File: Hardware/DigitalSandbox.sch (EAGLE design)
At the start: 82 parts, among them Q1 MOSFET-N, Q2 MOSFET-P, Q3 MOSFET-N, Q4 MOSFET-N, Q5 MOSFET-N, U1 MCP73831, U2 ATMEGA328, U3 C2031N-1A2-B10K-GP, U4 MCP9700, U5 FT232RLSSOP, U6 TEMT6000, U7 V_REG_LDOSMD, U8 LMV358, U9 MIC9.7MM, X1 USB-SMD-NS, Y1 8MHz

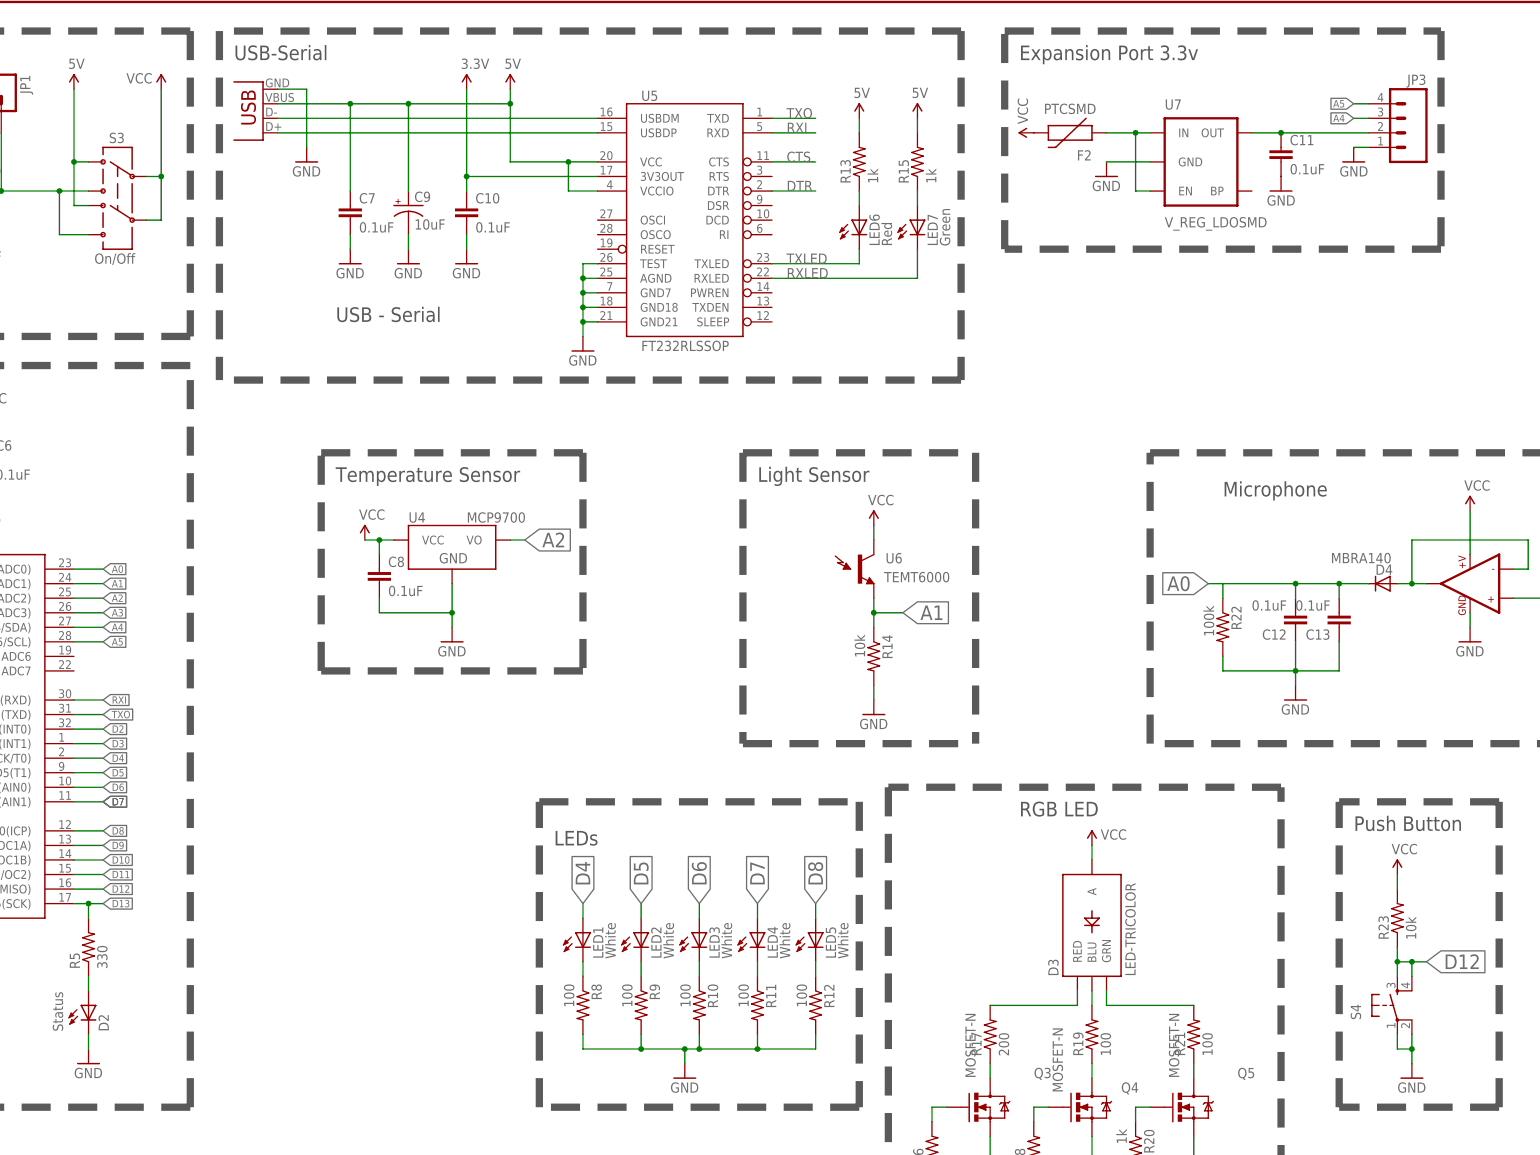
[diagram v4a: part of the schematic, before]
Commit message: Changes Made: 1. Swap Tx-Rx 3. correct stop mask on 2 exposed vias 6. flip default logic for push button (Currently normally high) 9. Change i2c header to meet new standard in the works.
TODO:
2. Make programming vias for Production
4. reverse the direction of the potentiometer and add silk showing "0 - 1024"
5. Source new push button
7. Investigate adding pulldown resistors for the nchannel fets that service the RGB led
8. Investigate a new resistor value for the light sensor to increase sensitivity.
10. Label pin 13 LED (near the uC).
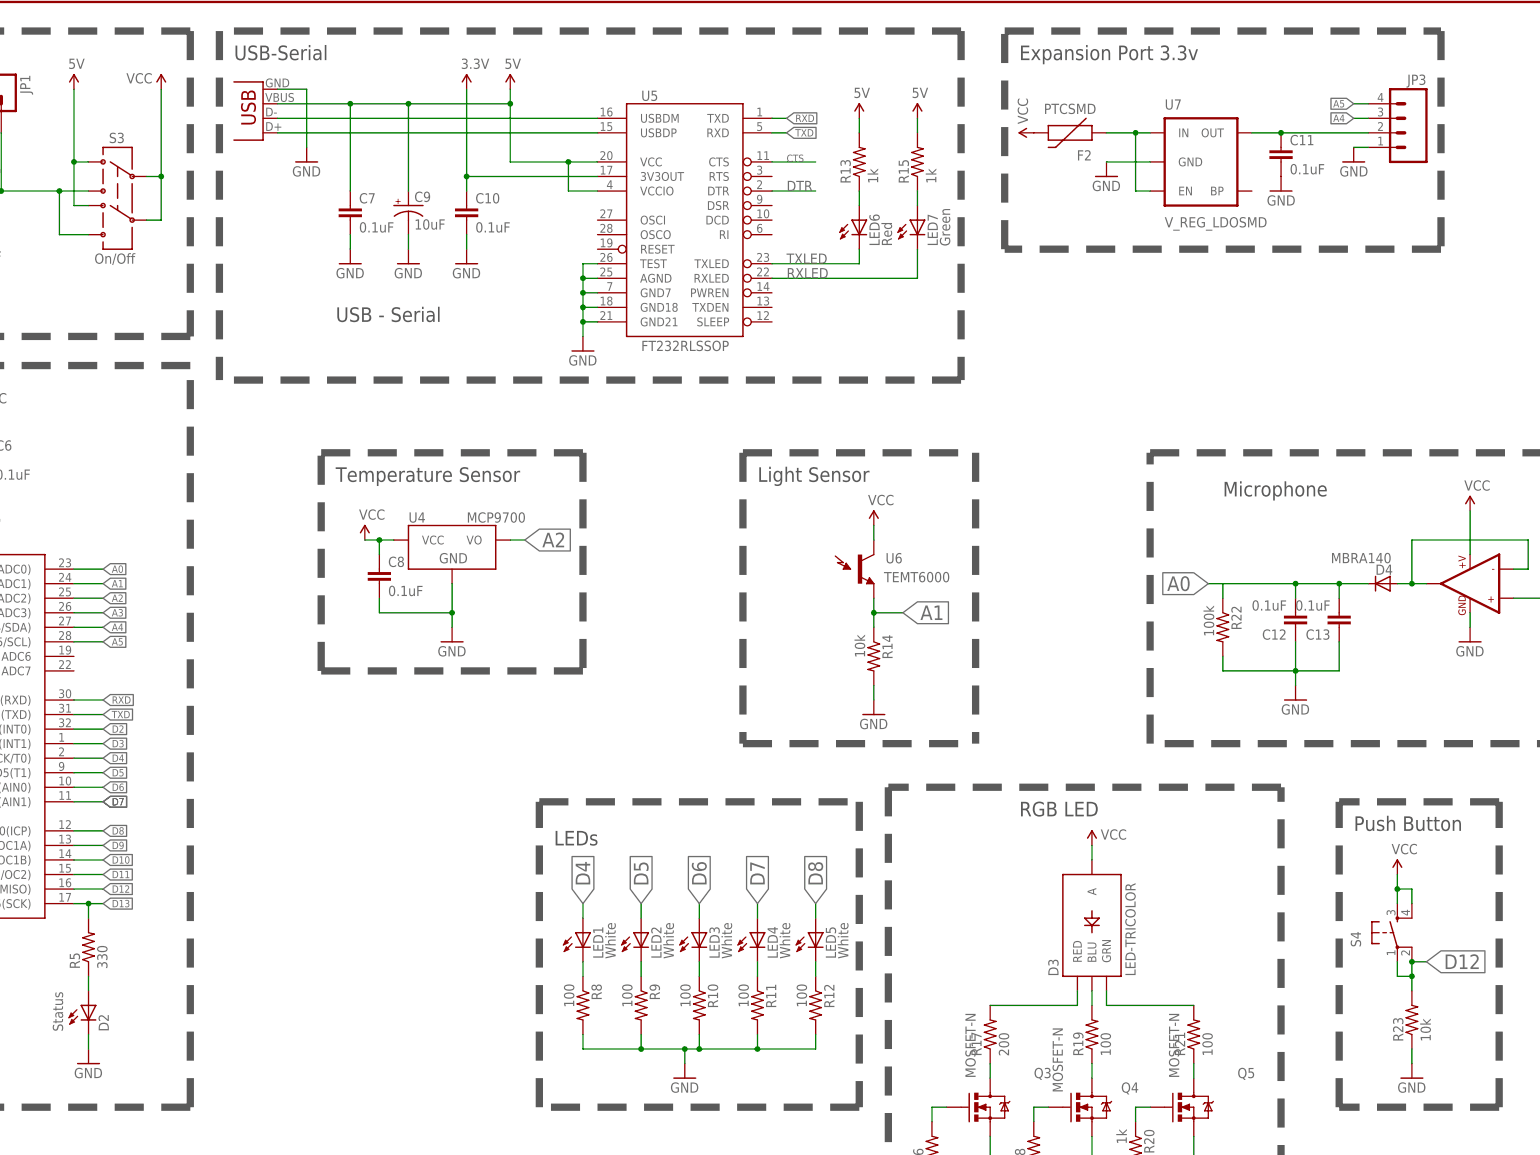
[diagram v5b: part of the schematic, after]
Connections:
- removed net RXI: U2.PD0(RXD), U5.RXD
- removed net TXO: U2.PD1(TXD), U5.TXD
- new net RXD: U2.PD0(RXD), U5.TXD
- new net TXD: U2.PD1(TXD), U5.RXD
- net D12: now also R23.2, S4.1, S4.2; no longer R23.1, S4.3, S4.4
- net GND: now also R23.1; no longer S4.1, S4.2
- net VCC: now also S4.3, S4.4; no longer R23.2
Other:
- moved on the sheet: R23, S4
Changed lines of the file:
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@@
 <?xml version="1.0" encoding="utf-8"?>
 <!DOCTYPE eagle SYSTEM "eagle.dtd">
-<eagle version="6.0">
+<eagle version="6.5.0">
 <drawing>
 <settings>
@@
 </instance>
 <instance part="S2" gate="G$1" x="20.32" y="-332.74" rot="MR90"/>
-<instance part="S4" gate="S" x="304.8" y="-261.62" rot="R90"/>
+<instance part="S4" gate="S" x="304.8" y="-248.92" rot="R90"/>
 <instance part="R8" gate="G$1" x="162.56" y="-261.62" rot="R270"/>
 <instance part="R9" gate="G$1" x="172.72" y="-261.62" rot="R270"/>
@@
 </instance>
 <instance part="GND14" gate="1" x="101.6" y="-340.36"/>
-<instance part="R23" gate="G$1" x="304.8" y="-246.38" rot="R90"/>
+<instance part="R23" gate="G$1" x="307.34" y="-264.16" rot="R90"/>
 <instance part="P+9" gate="1" x="304.8" y="-238.76" smashed="yes">
 <attribute name="VALUE" x="303.784" y="-235.204" size="1.778" layer="96"/>
@@
 </segment>
 <segment>
-<wire x1="307.34" y1="-269.24" x2="307.34" y2="-266.7" width="0.1524" layer="91"/>
-<pinref part="S4" gate="S" pin="2"/>
-<pinref part="S4" gate="S" pin="1"/>
-<wire x1="304.8" y1="-266.7" x2="304.8" y2="-269.24" width="0.1524" layer="91"/>
-<wire x1="304.8" y1="-269.24" x2="307.34" y2="-269.24" width="0.1524" layer="91"/>
 <pinref part="GND15" gate="1" pin="GND"/>
 <wire x1="307.34" y1="-271.78" x2="307.34" y2="-269.24" width="0.1524" layer="91"/>
-<junction x="307.34" y="-269.24"/>
+<pinref part="R23" gate="G$1" pin="1"/>
 </segment>
 <segment>
@@
 </segment>
 <segment>
-<pinref part="R23" gate="G$1" pin="2"/>
-<pinref part="P+9" gate="1" pin="VCC"/>
-<wire x1="304.8" y1="-238.76" x2="304.8" y2="-241.3" width="0.1524" layer="91"/>
-</segment>
-<segment>
 <wire x1="375.92" y1="-172.72" x2="375.92" y2="-175.26" width="0.1524" layer="91"/>
 <pinref part="P+12" gate="1" pin="VCC"/>
@@
 <pinref part="P+19" gate="1" pin="VCC"/>
 <pinref part="F2" gate="G$1" pin="2"/>
+</segment>
+<segment>
+<pinref part="S4" gate="S" pin="3"/>
+<pinref part="P+9" gate="1" pin="VCC"/>
+<wire x1="304.8" y1="-243.84" x2="304.8" y2="-241.3" width="0.1524" layer="91"/>
+<pinref part="S4" gate="S" pin="4"/>
+<wire x1="304.8" y1="-241.3" x2="304.8" y2="-238.76" width="0.1524" layer="91"/>
+<wire x1="307.34" y1="-243.84" x2="307.34" y2="-241.3" width="0.1524" layer="91"/>
+<wire x1="307.34" y1="-241.3" x2="304.8" y2="-241.3" width="0.1524" layer="91"/>
+<junction x="304.8" y="-241.3"/>
 </segment>
 </net>
@@
 </segment>
 </net>
-<net name="RXI" class="0">
+<net name="RXD" class="0">
 <segment>
 <wire x1="73.66" y1="-208.28" x2="78.74" y2="-208.28" width="0.1524" layer="91"/>
@@
 </segment>
 <segment>
-<wire x1="195.58" y1="-109.22" x2="203.2" y2="-109.22" width="0.1524" layer="91"/>
-<label x="198.12" y="-109.22" size="1.778" layer="95"/>
-<pinref part="U5" gate="G$1" pin="RXD"/>
-</segment>
-</net>
-<net name="TXO" class="0">
+<pinref part="U5" gate="G$1" pin="TXD"/>
+<wire x1="195.58" y1="-106.68" x2="198.12" y2="-106.68" width="0.1524" layer="91"/>
+<label x="198.12" y="-106.68" size="1.27" layer="95" xref="yes"/>
+</segment>
+</net>
+<net name="TXD" class="0">
 <segment>
 <wire x1="73.66" y1="-210.82" x2="78.74" y2="-210.82" width="0.1524" layer="91"/>
@@
 </segment>
 <segment>
-<wire x1="195.58" y1="-106.68" x2="203.2" y2="-106.68" width="0.1524" layer="91"/>
-<label x="198.12" y="-106.68" size="1.778" layer="95"/>
-<pinref part="U5" gate="G$1" pin="TXD"/>
+<pinref part="U5" gate="G$1" pin="RXD"/>
+<wire x1="195.58" y1="-109.22" x2="198.12" y2="-109.22" width="0.1524" layer="91"/>
+<label x="198.12" y="-109.22" size="1.27" layer="95" xref="yes"/>
 </segment>
 </net>
@@
 </segment>
 <segment>
-<pinref part="R23" gate="G$1" pin="1"/>
-<wire x1="304.8" y1="-251.46" x2="304.8" y2="-254" width="0.1524" layer="91"/>
-<pinref part="S4" gate="S" pin="4"/>
-<wire x1="304.8" y1="-254" x2="307.34" y2="-254" width="0.1524" layer="91"/>
-<wire x1="307.34" y1="-254" x2="307.34" y2="-256.54" width="0.1524" layer="91"/>
-<pinref part="S4" gate="S" pin="3"/>
-<wire x1="304.8" y1="-254" x2="304.8" y2="-256.54" width="0.1524" layer="91"/>
 <wire x1="307.34" y1="-254" x2="309.88" y2="-254" width="0.1524" layer="91"/>
 <label x="309.88" y="-254" size="2.54" layer="95" xref="yes"/>
+<pinref part="S4" gate="S" pin="2"/>
+<pinref part="R23" gate="G$1" pin="2"/>
+<wire x1="307.34" y1="-254" x2="307.34" y2="-256.54" width="0.1524" layer="91"/>
+<pinref part="S4" gate="S" pin="1"/>
+<wire x1="307.34" y1="-256.54" x2="307.34" y2="-259.08" width="0.1524" layer="91"/>
+<wire x1="304.8" y1="-254" x2="304.8" y2="-256.54" width="0.1524" layer="91"/>
+<wire x1="304.8" y1="-256.54" x2="307.34" y2="-256.54" width="0.1524" layer="91"/>
+<junction x="307.34" y="-256.54"/>
 <junction x="307.34" y="-254"/>
-<junction x="304.8" y="-254"/>
 </segment>
 </net>
@@
 <segment>
 <wire x1="195.58" y1="-114.3" x2="203.2" y2="-114.3" width="0.1524" layer="91"/>
-<label x="198.12" y="-114.3" size="1.778" layer="95"/>
+<label x="198.12" y="-114.3" size="1.27" layer="95"/>
 <pinref part="U5" gate="G$1" pin="CTS"/>
 </segment>

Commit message: Changes Made
1. Made programming vias for Production
2. reversed the direction of the potentiometer and added silk showing "0 - 1024"
3. Replaced Mosfets with NPN transistors to control RGB led
4. Replaces Light sensor with one used on Weather Shield IC-11836
5. Labeled pin 13 LED (near the uC).

TODO
1. Source new push button with better tactile feedback
2. Source new RGB Led that is diffused and common cathode (this would eliminate the need for transistors.
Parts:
- removed D4: MBRA140, SparkFun:DIODESMA
- removed R16, R18, R20: 1k, SparkFun-Passives:RESISTOR0603-RES
- removed U6: TEMT6000, SparkFun:TEMT6000
- added D5: (no value), SparkFun-DiscreteSemi:DIODESOD
- added U10: LIGHTSENSORALS, SparkFun-Sensors:LIGHTSENSORALS
- Q3, Q4, Q5: value MOSFET-N -> MMBT2222A; device SparkFun-DiscreteSemi:MOSFET-NCHANNELBSS138 -> SparkFun-DiscreteSemi:TRANSISTOR_NPNMMBT2222A; PROD_ID TRANS-00830 -> (none)
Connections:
- removed net N$14: Q3.G, R16.2
- removed net N$19: Q4.G, R18.2
- removed net N$22: Q5.G, R20.1
- net A0: now also D5.C; no longer D4.C
- net A1: now also U10.E1; no longer U6.E1
- net D10: now also Q4.B; no longer R18.1
- net D11: now also Q5.B; no longer R20.2
- net D9: now also Q3.B; no longer R16.1
- net GND: now also Q3.E, Q4.E, Q5.E; no longer Q3.S, Q4.S, Q5.S
- net N$24: now also D5.A; no longer D4.A
- net N$25: now also Q5.C; no longer Q5.D
- net N$27: now also Q4.C; no longer Q4.D
- net N$29: now also Q3.C; no longer Q3.D
- net VCC: now also U10.C1; no longer U6.C1
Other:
- note added: "v02"
- note removed: "v01"

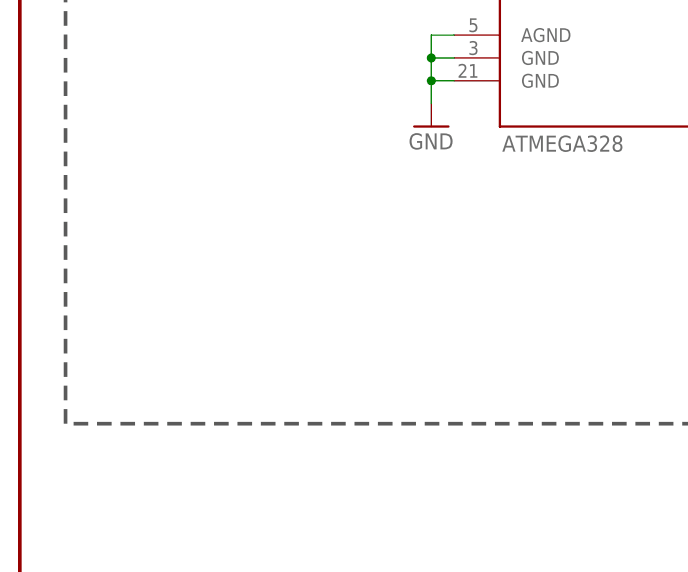
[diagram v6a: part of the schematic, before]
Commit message: added ISP header
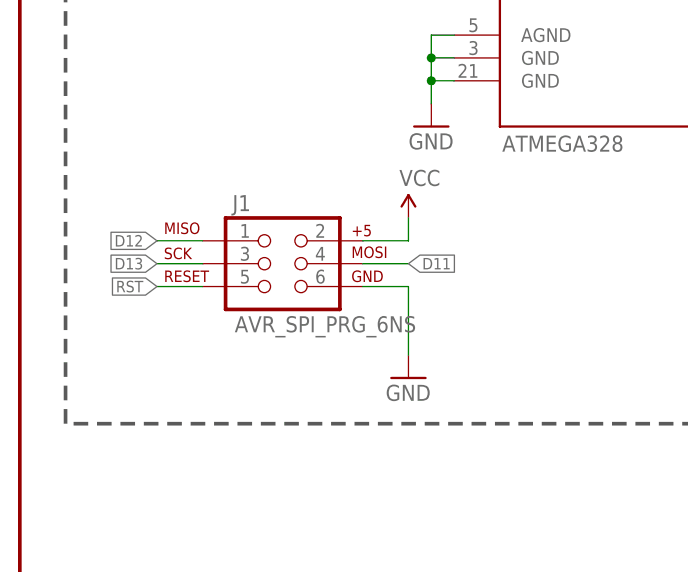
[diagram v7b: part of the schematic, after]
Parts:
- added J1: AVR_SPI_PRG_6NS, SparkFun-Connectors:AVR_SPI_PRG_6NS
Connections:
- net D11: now also J1.4
- net D12: now also J1.1
- net D13: now also J1.3
- net GND: now also J1.6
- net RST: now also J1.5
- net VCC: now also J1.2
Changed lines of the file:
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@@
 <layer number="91" name="Nets" color="2" fill="1" visible="yes" active="yes"/>
 <layer number="92" name="Busses" color="1" fill="1" visible="yes" active="yes"/>
-<layer number="93" name="Pins" color="2" fill="1" visible="yes" active="yes"/>
+<layer number="93" name="Pins" color="2" fill="1" visible="no" active="yes"/>
 <layer number="94" name="Symbols" color="4" fill="1" visible="yes" active="yes"/>
 <layer number="95" name="Names" color="7" fill="1" visible="yes" active="yes"/>
@@
 <part name="U10" library="SparkFun-Sensors" deviceset="LIGHTSENSOR" device="ALS"/>
 <part name="D5" library="SparkFun-DiscreteSemi" deviceset="DIODE" device="SOD"/>
+<part name="J1" library="SparkFun-Connectors" deviceset="AVR_SPI_PRG_6" device="NS"/>
+<part name="GND37" library="SparkFun" deviceset="GND" device=""/>
+<part name="P+20" library="SparkFun" deviceset="VCC" device=""/>
 </parts>
 <sheets>
@@
 <instance part="U10" gate="G$1" x="210.82" y="-185.42"/>
 <instance part="D5" gate="G$1" x="302.26" y="-187.96" rot="R180"/>
+<instance part="J1" gate="G$1" x="5.08" y="-261.62"/>
+<instance part="GND37" gate="1" x="20.32" y="-274.32"/>
+<instance part="P+20" gate="1" x="20.32" y="-256.54" smashed="yes">
+<attribute name="VALUE" x="19.304" y="-252.984" size="1.778" layer="96"/>
+</instance>
 </instances>
 <busses>
@@
 <pinref part="Q5" gate="G$1" pin="E"/>
 </segment>
+<segment>
+<pinref part="J1" gate="G$1" pin="6"/>
+<wire x1="15.24" y1="-264.16" x2="20.32" y2="-264.16" width="0.1524" layer="91"/>
+<wire x1="20.32" y1="-264.16" x2="20.32" y2="-271.78" width="0.1524" layer="91"/>
+<pinref part="GND37" gate="1" pin="GND"/>
+</segment>
 </net>
 <net name="VCC" class="1">
@@
 <junction x="304.8" y="-241.3"/>
 </segment>
+<segment>
+<pinref part="J1" gate="G$1" pin="2"/>
+<wire x1="15.24" y1="-259.08" x2="20.32" y2="-259.08" width="0.1524" layer="91"/>
+<wire x1="20.32" y1="-259.08" x2="20.32" y2="-256.54" width="0.1524" layer="91"/>
+<pinref part="P+20" gate="1" pin="VCC"/>
+</segment>
 </net>
 <net name="RST" class="0">
@@
 <wire x1="12.7" y1="-185.42" x2="12.7" y2="-187.96" width="0.1524" layer="91"/>
 </segment>
+<segment>
+<pinref part="J1" gate="G$1" pin="5"/>
+<wire x1="-2.54" y1="-264.16" x2="-7.62" y2="-264.16" width="0.1524" layer="91"/>
+<label x="-7.62" y="-264.16" size="1.27" layer="95" rot="R180" xref="yes"/>
+</segment>
 </net>
 <net name="D11" class="0">
@@
 <wire x1="259.08" y1="-279.4" x2="264.16" y2="-279.4" width="0.1524" layer="91"/>
 <pinref part="Q5" gate="G$1" pin="B"/>
+</segment>
+<segment>
+<pinref part="J1" gate="G$1" pin="4"/>
+<wire x1="15.24" y1="-261.62" x2="20.32" y2="-261.62" width="0.1524" layer="91"/>
+<label x="20.32" y="-261.62" size="1.27" layer="95" xref="yes"/>
 </segment>
 </net>
@@
 <junction x="76.2" y="-243.84"/>
 <label x="78.74" y="-243.84" size="1.27" layer="95" xref="yes"/>
+</segment>
+<segment>
+<pinref part="J1" gate="G$1" pin="3"/>
+<wire x1="-2.54" y1="-261.62" x2="-7.62" y2="-261.62" width="0.1524" layer="91"/>
+<label x="-7.62" y="-261.62" size="1.27" layer="95" rot="R180" xref="yes"/>
 </segment>
 </net>
@@
 <junction x="307.34" y="-254"/>
 </segment>
-</net>
+<segment>
+<pinref part="J1" gate="G$1" pin="1"/>
+<wire x1="-2.54" y1="-259.08" x2="-7.62" y2="-259.08" width="0.1524" layer="91"/>
+<label x="-7.62" y="-259.08" size="1.27" layer="95" rot="R180" xref="yes"/>
+</segment>
+</net>
